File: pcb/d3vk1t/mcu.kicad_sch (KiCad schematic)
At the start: 1 part, among them U1 STM32F412RETx

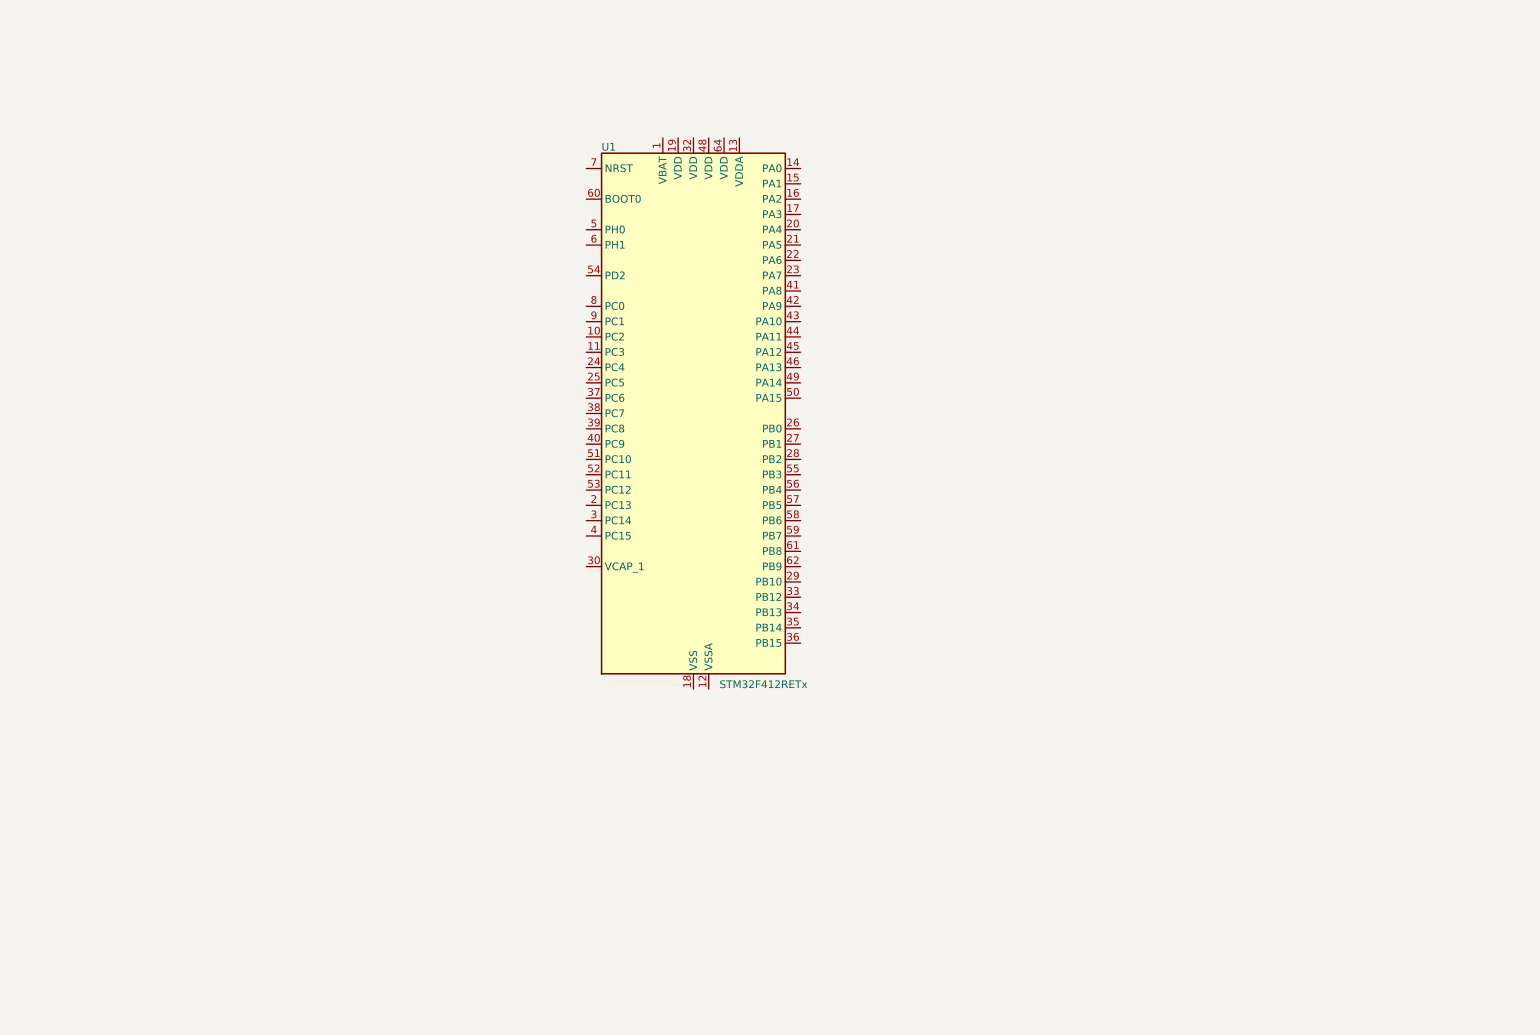
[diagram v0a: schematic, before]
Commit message: doc: added f4 hw dev doc
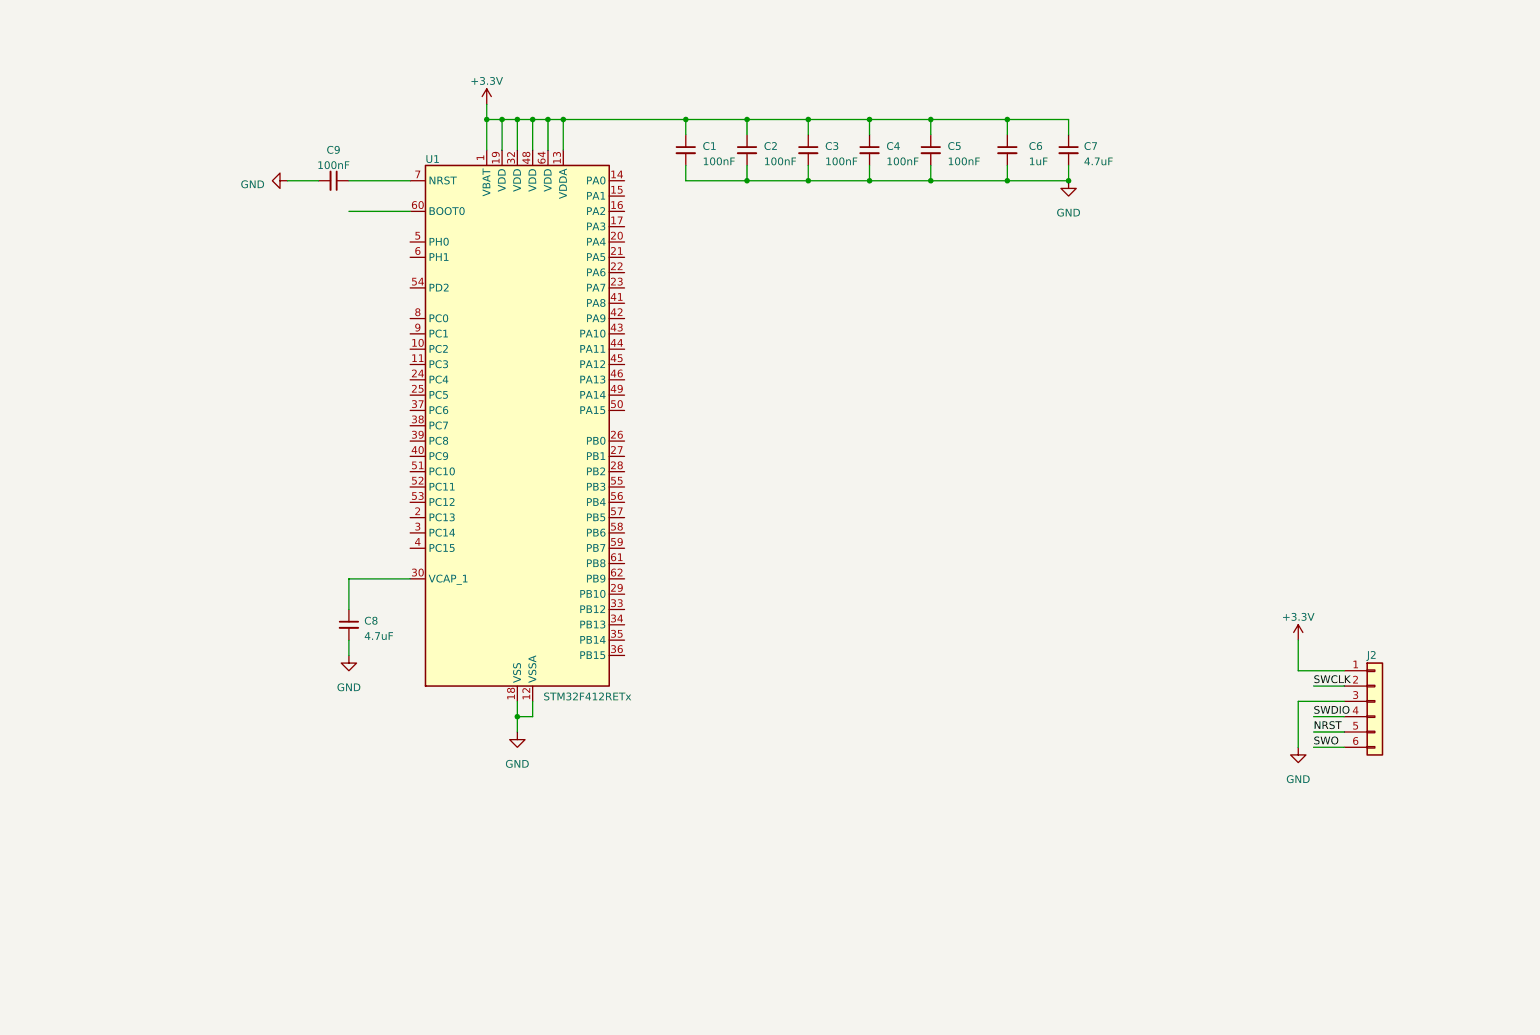
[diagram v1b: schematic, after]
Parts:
- added C1, C2, C3, C4, C5, C9: 100nF, Capacitor_SMD:C_0402_1005Metric, symbol Device:C_Small
- added C6: 1uF, Capacitor_SMD:C_0603_1608Metric, symbol Device:C_Small
- added C7, C8: 4.7uF, Capacitor_SMD:C_0603_1608Metric, symbol Device:C_Small
- added J2: Conn_01x06, Connector_PinHeader_2.54mm:PinHeader_1x06_P2.54mm_Vertical, symbol Connector_Generic:Conn_01x06
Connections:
- net +3.3V: now reaches U1.1 (VBAT)
- net +3.3V: now also U1.13 (VDDA), U1.19 (VDD), U1.32 (VDD), U1.48 (VDD), U1.64 (VDD), C1.1, C2.1, C3.1, C4.1, C5.1, C6.1, C7.1, J2.1 (Pin_1)
- net GND: now reaches U1.12 (VSSA)
- net GND: now also U1.18 (VSS), U1.31 (VSS), U1.47 (VSS), U1.63 (VSS), C1.2, C2.2, C3.2, C4.2, C5.2, C6.2, C7.2, C8.2, C9.2, J2.3 (Pin_3)
- net at U1.30 (VCAP_1): now also C8.1
- net at U1.7 (NRST): now also C9.1
- new net NRST: J2.5 (Pin_5)
- new net SWCLK: J2.2 (Pin_2)
- new net SWDIO: J2.4 (Pin_4)
- new net SWO: J2.6 (Pin_6)
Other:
- moved on the sheet: U1

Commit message: [update all schematics sheets]
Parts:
- added C15: 100nF, Capacitor_SMD:C_0402_1005Metric, symbol Device:C_Small
- added SW1 (x2): SW_Push, Button_Switch_SMD:SW_SPST_FSMSM, symbol Switch:SW_Push
- C8: value 4.7uF -> 2.2uF
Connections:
- net GND: now also C15.2, SW1.1, SW1.1
- net NRST: now also C9.1, U1.7 (NRST), SW1.2
- net SWCLK: now also U1.49 (PA14)
- net SWDIO: now also U1.46 (PA13)
- net SWO: now also U1.55 (PB3)
- net USER: now reaches U1.14 (PA0)
- net USER: now also C15.1, SW1.2
- net BOOT0: now reaches U1.60 (BOOT0)
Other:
- moved on the sheet: C1, C2, C3, C4, C5, C6, C7, C8, C9, U1

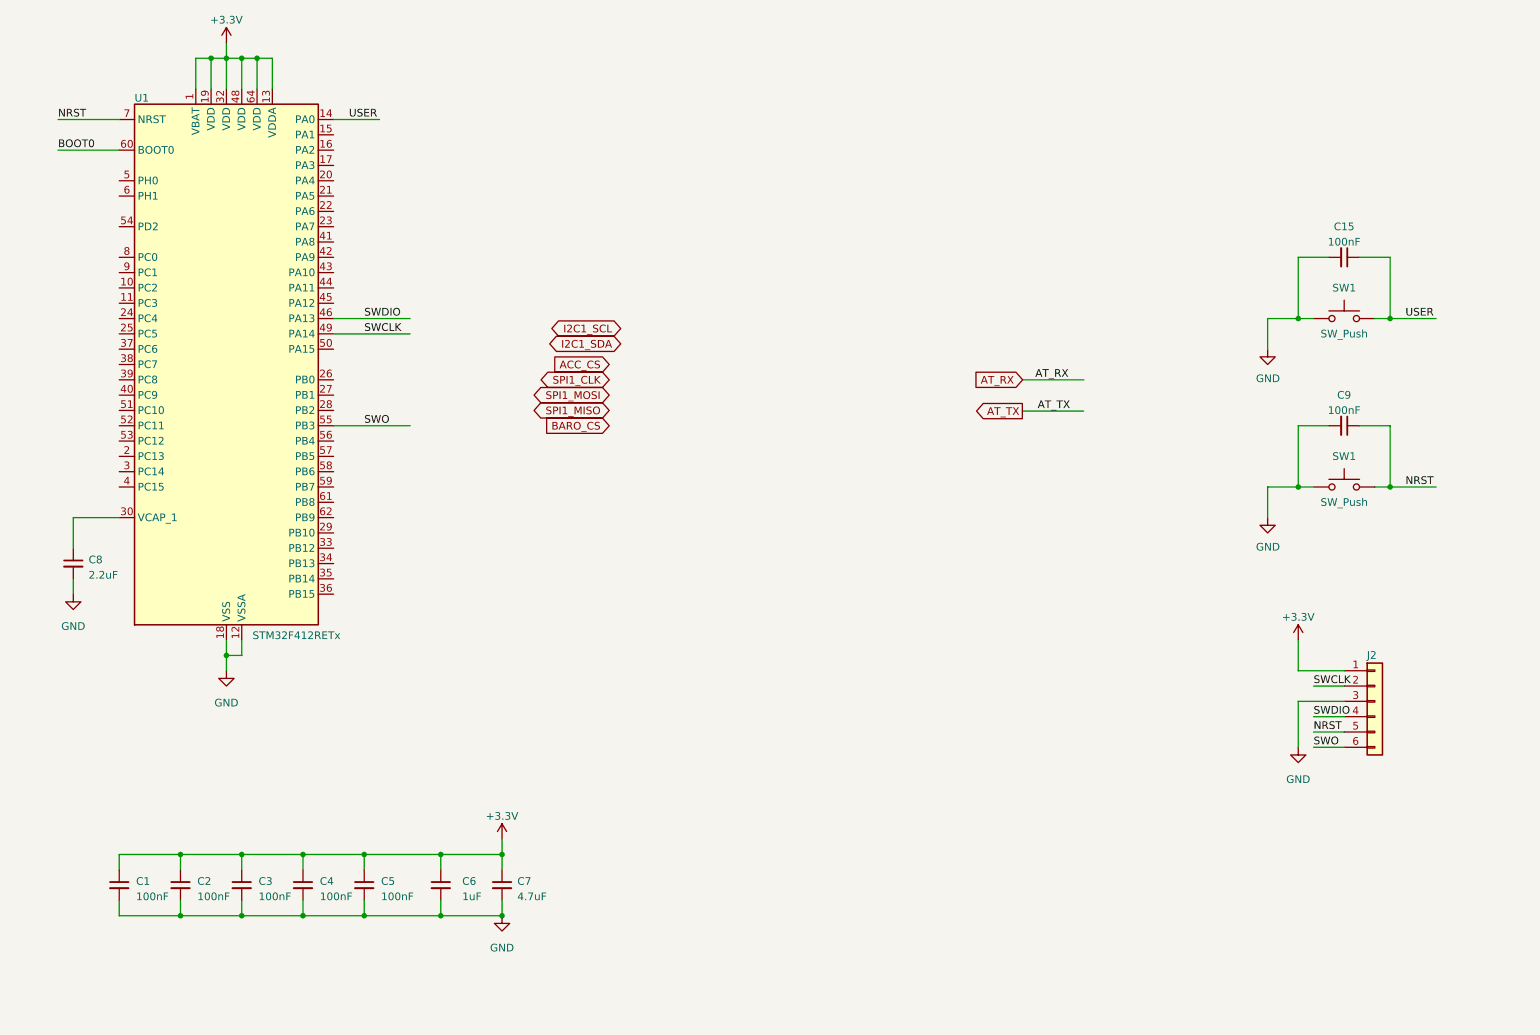
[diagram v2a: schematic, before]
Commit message: sch: update all sch sheets.
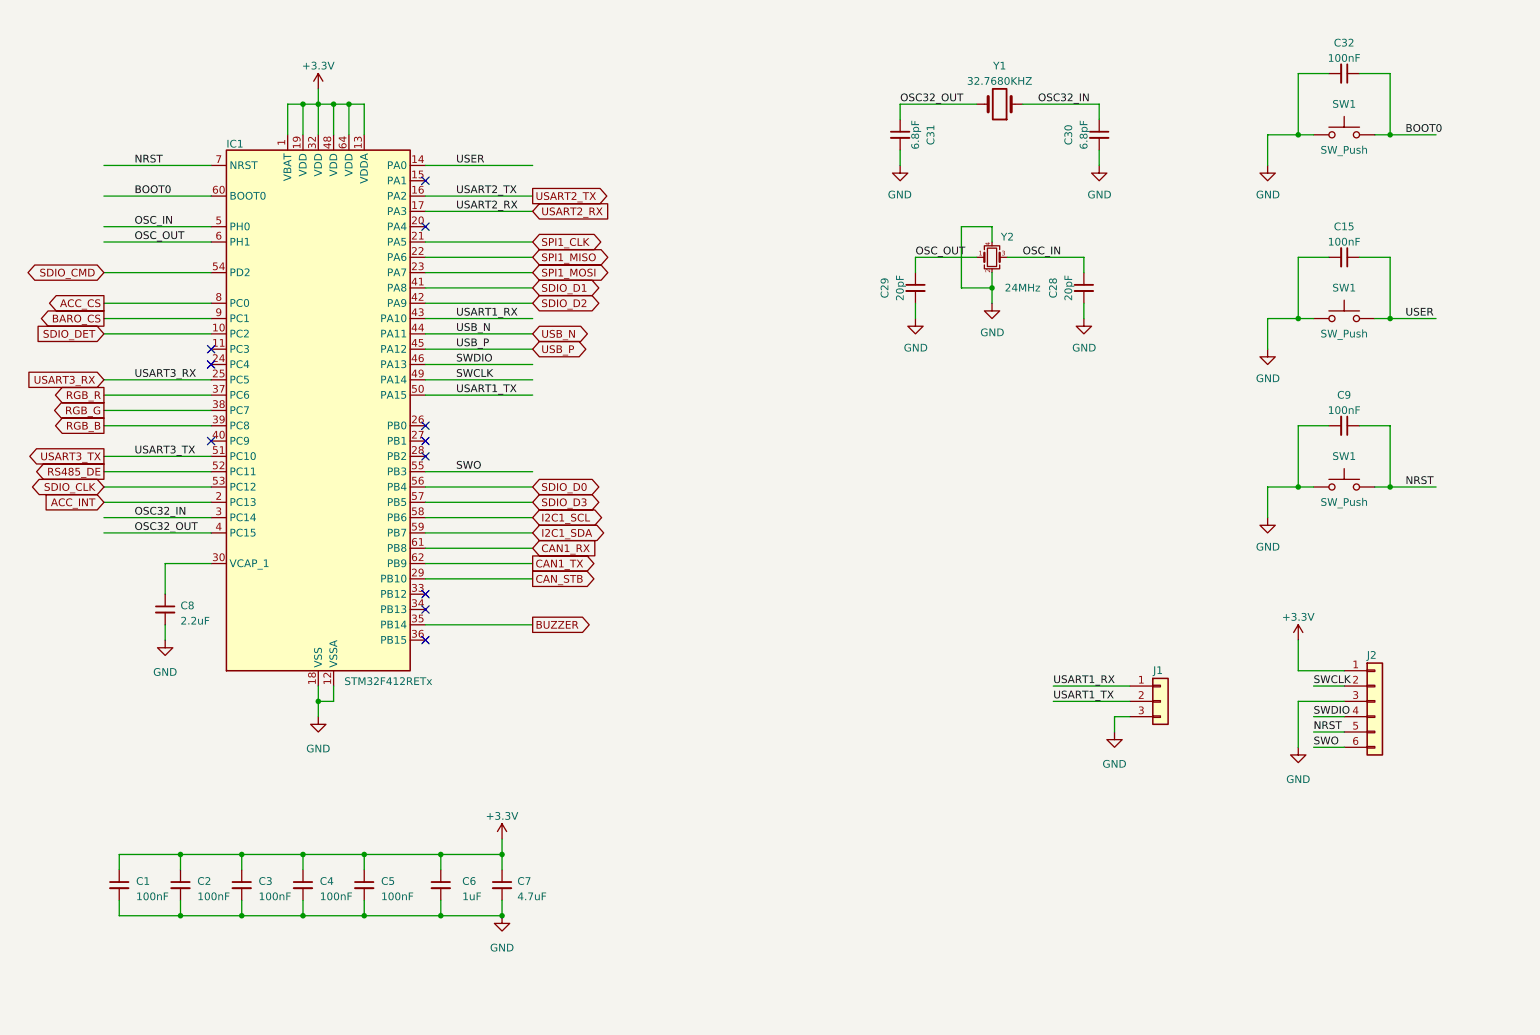
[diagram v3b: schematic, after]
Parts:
- added C28, C29: 20pF, Capacitor_SMD:C_0402_1005Metric, symbol Device:C_Small
- added C30, C31: 6.8pF, Capacitor_SMD:C_0402_1005Metric, symbol Device:C_Small
- added C32: 100nF, Capacitor_SMD:C_0402_1005Metric, symbol Device:C_Small
- added J1: Conn_01x03, Connector_PinHeader_2.54mm:PinHeader_1x03_P2.54mm_Vertical, symbol Connector_Generic:Conn_01x03
- added SW1: SW_Push, Button_Switch_SMD:SW_SPST_FSMSM, symbol Switch:SW_Push
- added Y1: 32.7680KHZ, Crystal:Crystal_SMD_EuroQuartz_EQ161-2Pin_3.2x1.5mm, symbol Device:Crystal
- added Y2: 24MHz, Crystal:Crystal_SMD_2016-4Pin_2.0x1.6mm, symbol Device:Crystal_GND24_Small
- renumbered U1 to IC1
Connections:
- net ACC_CS: now also IC1.8 (PC0)
- net BARO_CS: now also IC1.9 (PC1)
- net BOOT0: now also C32.1, SW1.2
- net GND: now also C28.2, C29.2, C30.2, C31.2, C32.2, J1.3 (Pin_3), SW1.1, Y2.2, Y2.4
- net I2C1_SCL: now also IC1.58 (PB6)
- net I2C1_SDA: now also IC1.59 (PB7)
- net SPI1_CLK: now also IC1.21 (PA5)
- net SPI1_MISO: now also IC1.22 (PA6)
- net SPI1_MOSI: now also IC1.23 (PA7)
- net SDIO_DET: now reaches IC1.10 (PC2)
- net USART2_TX: now reaches IC1.16 (PA2)
- net USART2_RX: now reaches IC1.17 (PA3)
- net ACC_INT: now reaches IC1.2 (PC13)
- net USART3_RX: now reaches IC1.25 (PC5)
- net CAN_STB: now reaches IC1.29 (PB10)
- net OSC32_IN: now reaches IC1.3 (PC14)
- net OSC32_IN: now also C30.1, Y1.1
- net BUZZER: now reaches IC1.35 (PB14)
- net RGB_R: now reaches IC1.37 (PC6)
- net RGB_G: now reaches IC1.38 (PC7)
- net RGB_B: now reaches IC1.39 (PC8)
- net OSC32_OUT: now reaches IC1.4 (PC15)
- net OSC32_OUT: now also C31.1, Y1.2
- net SDIO_D1: now reaches IC1.41 (PA8)
- net SDIO_D2: now reaches IC1.42 (PA9)
- net USART1_RX: now reaches IC1.43 (PA10)
- net USART1_RX: now also J1.1 (Pin_1)
- net USB_N: now reaches IC1.44 (PA11)
- net USB_P: now reaches IC1.45 (PA12)
- net OSC_IN: now reaches IC1.5 (PH0)
- net OSC_IN: now also C28.1, Y2.3
- net USART1_TX: now reaches IC1.50 (PA15)
- net USART1_TX: now also J1.2 (Pin_2)
- net USART3_TX: now reaches IC1.51 (PC10)
- net RS485_DE: now reaches IC1.52 (PC11)
- net SDIO_CLK: now reaches IC1.53 (PC12)
- net SDIO_CMD: now reaches IC1.54 (PD2)
- net SDIO_D0: now reaches IC1.56 (PB4)
- net SDIO_D3: now reaches IC1.57 (PB5)
- net OSC_OUT: now reaches IC1.6 (PH1)
- net OSC_OUT: now also C29.1, Y2.1
- net CAN1_RX: now reaches IC1.61 (PB8)
- net CAN1_TX: now reaches IC1.62 (PB9)
- no-connect marks 0 -> 11
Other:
- moved on the sheet: C8, IC1

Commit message: pcb: update layout
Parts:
- added R1: 10K, Resistor_SMD:R_0402_1005Metric, symbol Device:R_Small
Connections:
- net +3.3V: now also C32.2, SW1.1
- net BOOT0: now also R1.2
- net GND: now also R1.1; no longer C32.2, SW1.1
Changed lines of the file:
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@@
-    (stroke (width 0) (type default))
-  )
-  (wire (pts (xy 238.76 48.26) (xy 238.76 43.18))
     (stroke (width 0) (type default))
   )
@@
     (stroke (width 0) (type default))
   )
+  (wire (pts (xy 266.7 43.18) (xy 266.7 45.72))
+    (stroke (width 0) (type default))
+  )
   (wire (pts (xy 180.34 71.12) (xy 180.34 73.66))
     (stroke (width 0) (type default))
@@
   )
   (wire (pts (xy 45.72 88.9) (xy 63.5 88.9))
+    (stroke (width 0) (type default))
+  )
+  (wire (pts (xy 266.7 53.34) (xy 266.7 50.8))
     (stroke (width 0) (type default))
   )
@@
         (path "/4ea523ae-7c45-478e-a9cc-6f4833d1a9d5/0c7e2350-c710-4f8b-bffc-99ae7438d4de"
           (reference "J2") (unit 1)
+        )
+      )
+    )
+  )
+  (symbol (lib_id "power:+3.3V") (at 238.76 43.18 90) (unit 1)
+    (in_bom yes) (on_board yes) (dnp no) (fields_autoplaced)
+    (property "Reference" "#PWR072" (at 242.57 43.18 0)
+      (effects (font (size 1.27 1.27)) hide)
+    )
+    (property "Value" "+3.3V" (at 234.95 43.815 90)
+      (effects (font (size 1.27 1.27)) (justify left))
+    )
+    (property "Footprint" "" (at 238.76 43.18 0)
+      (effects (font (size 1.27 1.27)) hide)
+    )
+    (property "Datasheet" "" (at 238.76 43.18 0)
+      (effects (font (size 1.27 1.27)) hide)
+    )
+    (pin "1")
+    (instances
+      (project "d3vk1t"
+        (path "/4ea523ae-7c45-478e-a9cc-6f4833d1a9d5/0c7e2350-c710-4f8b-bffc-99ae7438d4de"
+          (reference "#PWR072") (unit 1)
+        )
+      )
+    )
+  )
+  (symbol (lib_id "Device:R_Small") (at 266.7 48.26 180) (unit 1)
+    (in_bom yes) (on_board yes) (dnp no)
+    (property "Reference" "R1" (at 264.16 48.26 90)
+      (effects (font (size 1.27 1.27)))
+    )
+    (property "Value" "10K" (at 269.24 48.26 90)
+      (effects (font (size 1.27 1.27)))
+    )
+    (property "Footprint" "Resistor_SMD:R_0402_1005Metric" (at 266.7 48.26 0)
+      (effects (font (size 1.27 1.27)) hide)
+    )
+    (property "Datasheet" "~" (at 266.7 48.26 0)
+      (effects (font (size 1.27 1.27)) hide)
+    )
+    (pin "1")
+    (pin "2")
+    (instances
+      (project "d3vk1t"
+        (path "/4ea523ae-7c45-478e-a9cc-6f4833d1a9d5/41f8e312-86c0-4917-8944-524577576fad"
+          (reference "R1") (unit 1)
+        )
+        (path "/4ea523ae-7c45-478e-a9cc-6f4833d1a9d5/0c7e2350-c710-4f8b-bffc-99ae7438d4de"
+          (reference "R25") (unit 1)
         )
       )
@@
     )
   )
-  (symbol (lib_id "power:GND") (at 238.76 48.26 0) (unit 1)
-    (in_bom yes) (on_board yes) (dnp no)
-    (property "Reference" "#PWR071" (at 238.76 54.61 0)
-      (effects (font (size 1.27 1.27)) hide)
-    )
-    (property "Value" "GND" (at 240.8099 53.1358 0)
+  (symbol (lib_id "power:GND") (at 266.7 53.34 0) (unit 1)
+    (in_bom yes) (on_board yes) (dnp no)
+    (property "Reference" "#PWR071" (at 266.7 59.69 0)
+      (effects (font (size 1.27 1.27)) hide)
+    )
+    (property "Value" "GND" (at 268.7499 58.2158 0)
       (effects (font (size 1.27 1.27)) (justify right))
     )
-    (property "Footprint" "" (at 238.76 48.26 0)
-      (effects (font (size 1.27 1.27)) hide)
-    )
-    (property "Datasheet" "" (at 238.76 48.26 0)
-      (effects (font (size 1.27 1.27)) hide)
-    )
+    (property "Footprint" "" (at 266.7 53.34 0)
+      (effects (font (size 1.27 1.27)) hide)
+    )
+    (property "Datasheet" "" (at 266.7 53.34 0)
+      (effects (font (size 1.27 1.27)) hide)
+    )

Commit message: project update  - update pcb layout.  - update schmatics sheets.  - added manufacturing files.  - added documentation files.
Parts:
- IC1: value STM32F412RETx -> STM32F412RET6
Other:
- note added: "BUTTONS"
- note added: "CRYSTALS"
- note added: "MCU DECOUPLING CAP'S"
- note added: "SHELL"
- note added: "STM32F412RET6"
- note added: "SWD"
- title: (none) -> Microcontroller
- moved on the sheet: C1, C15, C2, C28, C29, C3, C30, C31, C32, C4, C5, C6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
